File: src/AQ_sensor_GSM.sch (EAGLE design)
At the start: 49 parts, among them IC2 MCP73831/OT, J1 F-1X03-SIP-100-32, SW1 PCM12SMTR, SW2 PCM12SMTR, U2 TEXAS_INSTRUMENTS_SN74HC125TE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, U3 TEXAS_INSTRUMENTS_LM1117IMP-3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, X1 53048-08, X2 SIMLOCK-C707_10M006_512_2, X4 50 Ohms

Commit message: sorted DRC
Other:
- note added: "LAST UPDATE: 05/10/2020"
- note added: "sensors.AFRICA GSM"
- note removed: "LAST UPDATE: 21/5/2020"
- note removed: "sensors.AFRICA MRC"
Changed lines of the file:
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@@
 <setting verticaltext="up"/>
 </settings>
-<grid distance="0.01" unitdist="inch" unit="inch" style="dots" multiple="1" display="yes" altdistance="0.01" altunitdist="inch" altunit="inch"/>
+<grid distance="0.1" unitdist="inch" unit="inch" style="lines" multiple="1" display="no" altdistance="0.01" altunitdist="inch" altunit="inch"/>
 <layers>
 <layer number="1" name="Top" color="4" fill="1" visible="no" active="no"/>
@@
 </layers>
 <schematic xreflabel="%F%N/%S.%C%R" xrefpart="/%S.%C%R">
-<fusionteam huburn="a.YnVzaW5lc3M6Y29kZWZvcmFmcmljYTE" projecturn="a.YnVzaW5lc3M6Y29kZWZvcmFmcmljYTEjMjAyMDAzMTgyNzU5ODExNzY" folderUrn="urn:adsk.wipprod:fs.folder:co.JvkIyPCGSUOTXoHwebdYWw" urn="urn:adsk.wipprod:dm.lineage:lKNtYnu6R0Wf073pCdF1XA"  versionUrn="urn:adsk.wipprod:fs.file:vf.lKNtYnu6R0Wf073pCdF1XA?version=5" camFileUrn="" camFileVersionUrn="" lastpublishedchangeguid="f7d3d892-1735-423b-440c-40111b257b6f"/>
+<fusionteam huburn="a.YnVzaW5lc3M6Y29kZWZvcmFmcmljYTE" projecturn="a.YnVzaW5lc3M6Y29kZWZvcmFmcmljYTEjMjAyMTEwMDU0NTIxNTU1MjY" folderUrn="urn:adsk.wipprod:fs.folder:co.V4eMQQrZRL-wTqnvGmJ6Nw" urn="urn:adsk.wipprod:dm.lineage:oPbGj42BQ0a8HHDQHNPmBg"  versionUrn="urn:adsk.wipprod:fs.file:vf.oPbGj42BQ0a8HHDQHNPmBg?version=1" camFileUrn="" camFileVersionUrn="" lastpublishedchangeguid="5f9c7e05-69a6-917d-ed76-c49c2c223d44"/>
 <attributes>
 </attributes>
@@
 <part name="GND2" library="supply1" library_urn="urn:adsk.eagle:library:371" deviceset="GND" device=""/>
 <part name="X1" library="AQ_sensor_GSM" library_urn="urn:adsk.eagle:library:30300195" deviceset="53?-08" device="048" package3d_urn="urn:adsk.eagle:package:30300278/2"/>
-<part name="J1" library="AQ_sensor_GSM" library_urn="urn:adsk.eagle:library:30300195" deviceset="F-1X03-" device="SIP-100-32" package3d_urn="urn:adsk.eagle:package:30300264/2"/>
+<part name="J1" library="AQ_sensor_GSM" library_urn="urn:adsk.eagle:library:30300195" deviceset="F-1X03-" device="SIP-100-32" package3d_urn="urn:adsk.eagle:package:30300264/3"/>
 <part name="SV1" library="AQ_sensor_GSM" library_urn="urn:adsk.eagle:library:30300195" deviceset="FE15-1" device="" package3d_urn="urn:adsk.eagle:package:30300273/2"/>
 <part name="SV2" library="AQ_sensor_GSM" library_urn="urn:adsk.eagle:library:30300195" deviceset="FE15-1" device="" package3d_urn="urn:adsk.eagle:package:30300273/2"/>
@@
 <sheet>
 <plain>
-<text x="294.64" y="15.24" size="1.778" layer="94">sensors.AFRICA MRC</text>
-<text x="345.44" y="10.16" size="1.778" layer="94">LAST UPDATE: 21/5/2020</text>
+<text x="294.64" y="15.24" size="1.778" layer="94">sensors.AFRICA GSM</text>
+<text x="345.44" y="10.16" size="1.778" layer="94">LAST UPDATE: 05/10/2020</text>
 <wire x1="5.08" y1="5.08" x2="111.76" y2="5.08" width="0.1524" layer="94" style="shortdash"/>
 <wire x1="5.08" y1="48.26" x2="5.08" y2="5.08" width="0.1524" layer="94" style="shortdash"/>

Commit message: Organized schematic
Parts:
- removed H1, H2, H3, H4: MOUNT-PAD-ROUND2.8, AQ_sensor_GSM:MOUNT-PAD-ROUND2.8
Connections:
- net GND: no longer H1.MOUNT, H2.MOUNT, H3.MOUNT, H4.MOUNT
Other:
- moved on the sheet: C1, C8, J1, MICRO_USB, POWER, R14, R5, SV1, SV2, SW1, U3, X1-1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

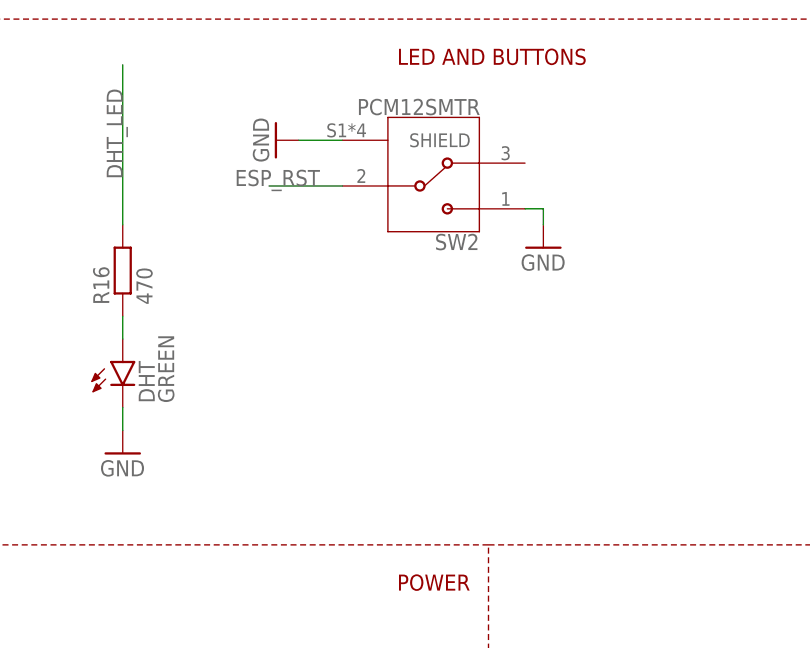
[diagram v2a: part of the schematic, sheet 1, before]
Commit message: Feature: Change components' positions.
1. Rotate NodeMCU 90 degrees anti-clockwise. 2. Add  onboard GSM Antenna. 3. Move Simcard Holder to top Layer. 4. Change Reset button to push button. 5. Rearrange Charging Circuitry layout to minimise trace resistance.
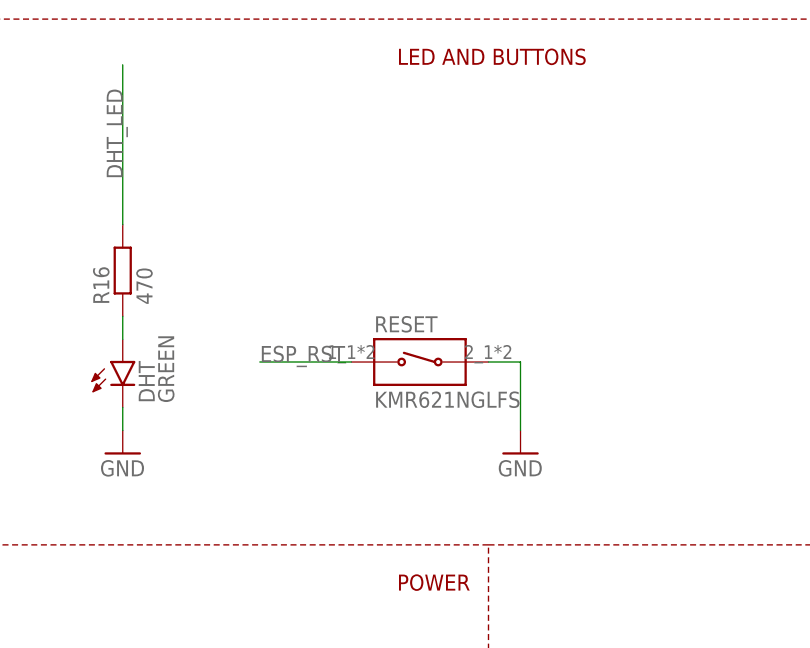
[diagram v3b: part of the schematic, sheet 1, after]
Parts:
- removed SW2: PCM12SMTR, AQ_sensor_GSM:PCM12SMTR
- added JP1: PINHD-1X1, Connector:PINHD-1X1
- added RESET: KMR621NGLFS, KMR621NGLFS:KMR621NGLFS
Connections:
- net ESP_RST: now also RESET.1; no longer SW2.2
- net GND: now also RESET.2; no longer SW2.1, SW2.SHIELD
- net GSM_ANT: now also JP1.1
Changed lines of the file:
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@@
 <part name="GND34" library="supply1" library_urn="urn:adsk.eagle:library:371" deviceset="GND" device=""/>
 <part name="FRAME1" library="frames" library_urn="urn:adsk.eagle:library:229" deviceset="A3L-LOC" device=""/>
-<part name="GND13" library="supply1" library_urn="urn:adsk.eagle:library:371" deviceset="GND" device=""/>
 <part name="DHT" library="led" library_urn="urn:adsk.eagle:library:259" deviceset="LED" device="CHIP-LED0603" package3d_urn="urn:adsk.eagle:package:15819/3" value="GREEN"/>
 <part name="R16" library="rcl" library_urn="urn:adsk.eagle:library:334" deviceset="R-EU_" device="R0603" package3d_urn="urn:adsk.eagle:package:23555/3" value="470"/>
 <part name="GND37" library="supply1" library_urn="urn:adsk.eagle:library:371" deviceset="GND" device=""/>
 <part name="SW1" library="AQ_sensor_GSM" library_urn="urn:adsk.eagle:library:30300195" deviceset="PCM12SMTR" device="" package3d_urn="urn:adsk.eagle:package:30300294/2"/>
-<part name="SW2" library="AQ_sensor_GSM" library_urn="urn:adsk.eagle:library:30300195" deviceset="PCM12SMTR" device="" package3d_urn="urn:adsk.eagle:package:30300294/2"/>
-<part name="GND12" library="supply1" library_urn="urn:adsk.eagle:library:371" deviceset="GND" device=""/>
 <part name="FRAME2" library="frames" library_urn="urn:adsk.eagle:library:229" deviceset="A3L-LOC" device=""/>
 <part name="U1" library="AQ_sensor_GSM" library_urn="urn:adsk.eagle:library:30300195" deviceset="GSM_SIM800L" device="" package3d_urn="urn:adsk.eagle:package:30300265/2"/>
@@
 <part name="+3V1" library="supply1" library_urn="urn:adsk.eagle:library:371" deviceset="+3V3" device=""/>
 <part name="+3V2" library="supply1" library_urn="urn:adsk.eagle:library:371" deviceset="+3V3" device=""/>
+<part name="JP1" library="Connector" library_urn="urn:adsk.eagle:library:16378166" deviceset="PINHD-1X1" device="" package3d_urn="urn:adsk.eagle:package:22485/2"/>
+<part name="RESET" library="KMR621NGLFS" deviceset="KMR621NGLFS" device="" override_package3d_urn="urn:adsk.eagle:package:41127407/2" override_package_urn="urn:adsk.eagle:footprint:41127408/1"/>
+<part name="GND11" library="supply1" library_urn="urn:adsk.eagle:library:371" deviceset="GND" device=""/>
 </parts>
 <sheets>
@@
 <attribute name="SHEET" x="357.505" y="5.08" size="2.54" layer="94"/>
 </instance>
-<instance part="GND13" gate="1" x="136.398" y="237.998" smashed="yes" rot="R270">
-<attribute name="VALUE" x="133.858" y="240.538" size="1.778" layer="96" rot="R270"/>
-</instance>
 <instance part="DHT" gate="G$1" x="119.38" y="213.36" smashed="yes">
 <attribute name="NAME" x="122.936" y="208.788" size="1.778" layer="95" rot="R90"/>
@@
 <attribute name="VALUE" x="51.91735" y="178.825859375" size="1.778459375" layer="96" rot="R180"/>
 </instance>
-<instance part="SW2" gate="G$1" x="153.924" y="232.918" smashed="yes" rot="R180">
-<attribute name="NAME" x="159.008390625" y="227.579390625" size="1.779540625" layer="95" rot="R180"/>
-<attribute name="VALUE" x="159.10535" y="242.579859375" size="1.778459375" layer="96" rot="R180"/>
-</instance>
-<instance part="GND12" gate="1" x="166.116" y="226.06" smashed="yes">
-<attribute name="VALUE" x="163.576" y="223.52" size="1.778" layer="96"/>
-</instance>
 <instance part="GND8" gate="1" x="96.52" y="201.93" smashed="yes">
 <attribute name="VALUE" x="93.98" y="199.39" size="1.778" layer="96"/>
@@
 <instance part="+3V2" gate="G$1" x="270.256" y="215.392" smashed="yes" rot="R180">
 <attribute name="VALUE" x="272.796" y="220.472" size="1.778" layer="96" rot="R270"/>
+</instance>
+<instance part="RESET" gate="G$1" x="152.4" y="213.36" smashed="yes">
+<attribute name="NAME" x="147.32" y="216.662" size="1.778" layer="95"/>
+<attribute name="VALUE" x="147.32" y="208.28" size="1.778" layer="96"/>
+</instance>
+<instance part="GND11" gate="1" x="163.576" y="203.2" smashed="yes">
+<attribute name="VALUE" x="161.036" y="200.66" size="1.778" layer="96"/>
 </instance>
 </instances>
@@
 </segment>
 <segment>
-<pinref part="GND13" gate="1" pin="GND"/>
-<pinref part="SW2" gate="G$1" pin="SHIELD"/>
-<wire x1="138.938" y1="237.998" x2="143.764" y2="237.998" width="0.1524" layer="91"/>
-</segment>
-<segment>
-<pinref part="SW2" gate="G$1" pin="1"/>
-<pinref part="GND12" gate="1" pin="GND"/>
-<wire x1="164.084" y1="230.378" x2="166.116" y2="230.378" width="0.1524" layer="91"/>
-<wire x1="166.116" y1="230.378" x2="166.116" y2="228.6" width="0.1524" layer="91"/>
-</segment>
-<segment>
 <pinref part="PMS" gate="G$1" pin="C"/>
 <wire x1="96.52" y1="208.28" x2="96.52" y2="204.47" width="0.1524" layer="91"/>
 <pinref part="GND8" gate="1" pin="GND"/>
+</segment>
+<segment>
+<pinref part="GND11" gate="1" pin="GND"/>
+<wire x1="163.576" y1="205.74" x2="163.576" y2="213.36" width="0.1524" layer="91"/>
+<pinref part="RESET" gate="G$1" pin="2"/>
+<wire x1="163.576" y1="213.36" x2="160.02" y2="213.36" width="0.1524" layer="91"/>
 </segment>
 </net>
@@
 </segment>
 <segment>
-<pinref part="SW2" gate="G$1" pin="2"/>
-<wire x1="143.764" y1="232.918" x2="135.636" y2="232.918" width="0.1524" layer="91"/>
-<label x="131.826" y="232.918" size="1.778" layer="95"/>
+<pinref part="RESET" gate="G$1" pin="1"/>
+<wire x1="144.78" y1="213.36" x2="134.62" y2="213.36" width="0.1524" layer="91"/>
+<label x="134.62" y="213.36" size="1.778" layer="95"/>
 </segment>
 </net>
@@
 <attribute name="VALUE" x="266.192" y="120.65" size="1.778" layer="96" rot="R180"/>
 </instance>
+<instance part="JP1" gate="G$1" x="256.54" y="76.2" smashed="yes" rot="R180">
+<attribute name="NAME" x="262.89" y="73.025" size="1.778" layer="95" rot="R180"/>
+<attribute name="VALUE" x="262.89" y="81.28" size="1.778" layer="96" rot="R180"/>
+</instance>
 </instances>
 <busses>
@@
 <wire x1="280.416" y1="103.378" x2="288.29" y2="103.378" width="0.1524" layer="91"/>
 <label x="280.924" y="104.14" size="1.778" layer="95"/>
+</segment>
+<segment>
+<pinref part="JP1" gate="G$1" pin="1"/>
+<wire x1="259.08" y1="76.2" x2="271.78" y2="76.2" width="0.1524" layer="91"/>
+<label x="266.7" y="76.2" size="1.778" layer="95"/>
 </segment>
 </net>
@@
 packages will not be understood (or retained) with this version.
 </note>
+<note version="9.4" severity="warning">
+Since Version 9.4, EAGLE supports the overriding of 3D packages
+in schematics and board files. Those overridden 3d packages
+will not be understood (or retained) with this version.
+</note>
 <note version="8.4" severity="warning">
